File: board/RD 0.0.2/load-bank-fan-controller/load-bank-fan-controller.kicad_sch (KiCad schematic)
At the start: 45 parts, among them J1 FAN1, J2 FAN2, J3 FAN3, J4 SPI, J5 UART, J6 12V IN, J7 TEMP1, J8 TEMP2, J9 RELAY, Q1 IRLML0030, Q2 IRLML0030, SW1 RESET, U1 AMS1117-5.0, U2 ATmega328P-A, U3 LM2904, Y1 Crystal

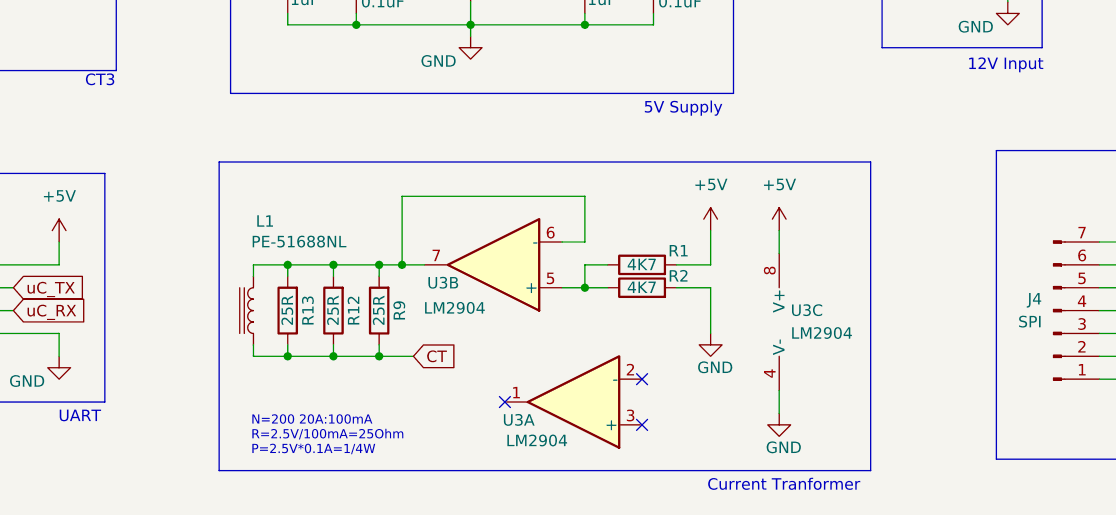
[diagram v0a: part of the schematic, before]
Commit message: replace current sense resistor with the proper one
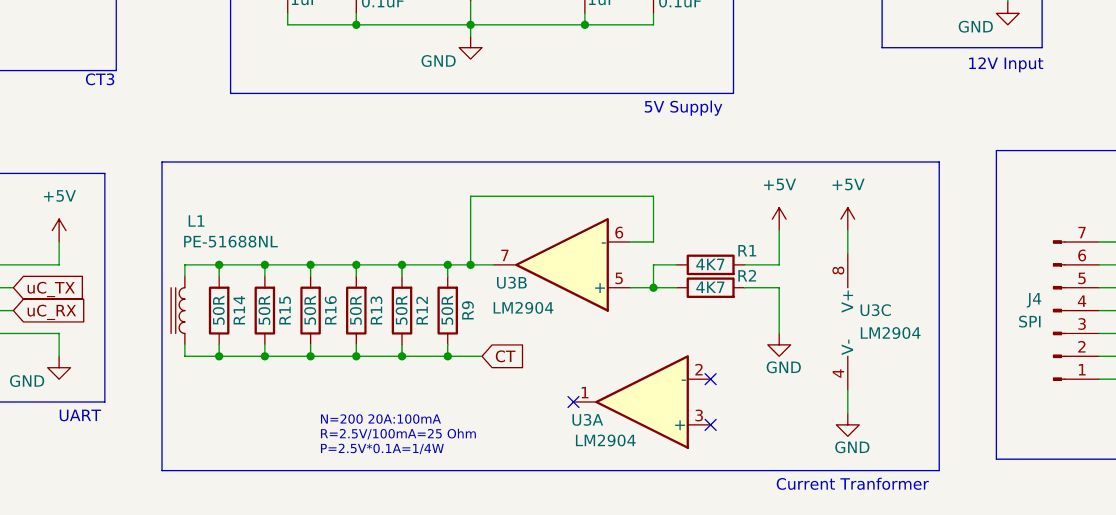
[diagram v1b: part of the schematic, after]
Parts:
- added R14, R15, R16: 50R, Resistor_SMD:R_MiniMELF_MMA-0204, symbol Device:R
- R12, R13, R9: value 25R -> 50R; footprint Resistor_SMD:R_0603_1608Metric_Pad0.98x0.95mm_HandSolder -> Resistor_SMD:R_MiniMELF_MMA-0204; LCSC Part # C99782 -> C489412; Manufacturer YAGEO -> Viking Tech; Mfg PN RC0603FR-074K7L -> CSR0204FTDV0500
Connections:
- net CT: now also R14.1, R15.1, R16.1
- net at L1.2, R12.2, R13.2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: now also R14.2, R15.2, R16.2
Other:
- note added: "N=200 20A:100mA R=2.5V/100mA=25 Ohm P=2.5V*0.1A=1/4W"
- note removed: "N=200 20A:100mA R=2.5V/100mA=25Ohm P=2.5V*0.1A=1/4W"
- moved on the sheet: R1, R12, R13, R2, R9, U3A, U3B, U3C

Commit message: connector changed and component added
change 12v connector, change spi to icsp connector, change  regulator input cap to 100u, remove uart conn, add diode to regulator input
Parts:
- removed J4: SPI, Connector_PinHeader_2.54mm:PinHeader_1x07_P2.54mm_Vertical, symbol Connector:Conn_01x07_Pin
- removed J5: UART, Connector_PinHeader_2.54mm:PinHeader_1x04_P2.54mm_Vertical, symbol Connector:Conn_01x04_Pin
- removed J6: 12V IN, TerminalBlock_RND:TerminalBlock_RND_205-00232_1x02_P5.08mm_Horizontal, symbol Connector:Conn_01x02_Pin
- added D3: 1N4007, Diode_SMD:D_SOD-123F, symbol Device:D
- added J6: ISP, Connector_PinHeader_2.54mm:PinHeader_2x03_P2.54mm_Vertical, symbol Connector:Conn_01x06_Pin
- added J8: 12V IN, Connector_JST:JST_VH_B3P-VH-B_1x03_P3.96mm_Vertical, symbol Connector:Conn_01x03_Pin
- C7: renamed from C1; value 1uF -> 100uF; footprint Capacitor_SMD:C_0603_1608Metric_Pad1.08x0.95mm_HandSolder -> Inductor_SMD:L_1210_3225Metric; LCSC Part # C14664 -> C394395; Manufacturer YAGEO -> Taiyo Yuden; Mfg PN CC0603KRX5R8BB105 -> EMK325ABJ107MM-T
- renumbered C6 to C1, C4 to C10, C7 to C2, C8 to C3, C5 to C4, C9 to C5, C10 to C6, C2 to C8, C3 to C9, D2 to D1, D3 to D2, DRA2 to DRA1, DRA1 to DRA2, J7 to J2, J9 to J3, J8 to J4, J2 to J5, J3 to J7, Q2 to Q1, Q1 to Q2, R5 to R1, R2 to R10, R14 to R11, R15 to R12, R16 to R13, R13 to R14, R12 to R15, R9 to R16, R10 to R2, R11 to R3, R8 to R4, R6 to R5, R7 to R6, R3 to R7, R4 to R8, R1 to R9, U2 to U1, U1 to U2
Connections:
- net +12V: now also D3.2 (A), J8.2 (Pin_2); no longer C7.1, C8.1, U2.3 (VI)
- net +5V: now also J6.2 (Pin_2)
- net GND: now also J6.6 (Pin_6), J8.3 (Pin_3)
- net MISO: now also J6.1 (Pin_1)
- net MOSI: now also J6.4 (Pin_4)
- net RESET: now also J6.5 (Pin_5)
- net SCK: now also J6.3 (Pin_3)
- new net +12VA: C7.1, C8.1, D3.1 (K), U2.3 (VI)
- no-connect marks 3 -> 4
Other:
- note removed: "UART"
- moved on the sheet: DRA1, DRA2, L1, R10, R11, R12, R13, R14, R15, R16, R9, U3A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

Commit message: change wrong footprint from L_1210 to C_1210
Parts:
- C7: footprint Inductor_SMD:L_1210_3225Metric -> Capacitor_SMD:C_1210_3225Metric
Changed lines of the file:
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@@
 			)
 		)
-		(property "Footprint" "Inductor_SMD:L_1210_3225Metric"
+		(property "Footprint" "Capacitor_SMD:C_1210_3225Metric"
 			(at 68.2752 142.24 0)
 			(effects
